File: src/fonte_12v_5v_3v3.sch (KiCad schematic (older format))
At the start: 10 parts, among them P3 12V Connector, U2 LD1117S50CTR, U3 LD1117S33CTR

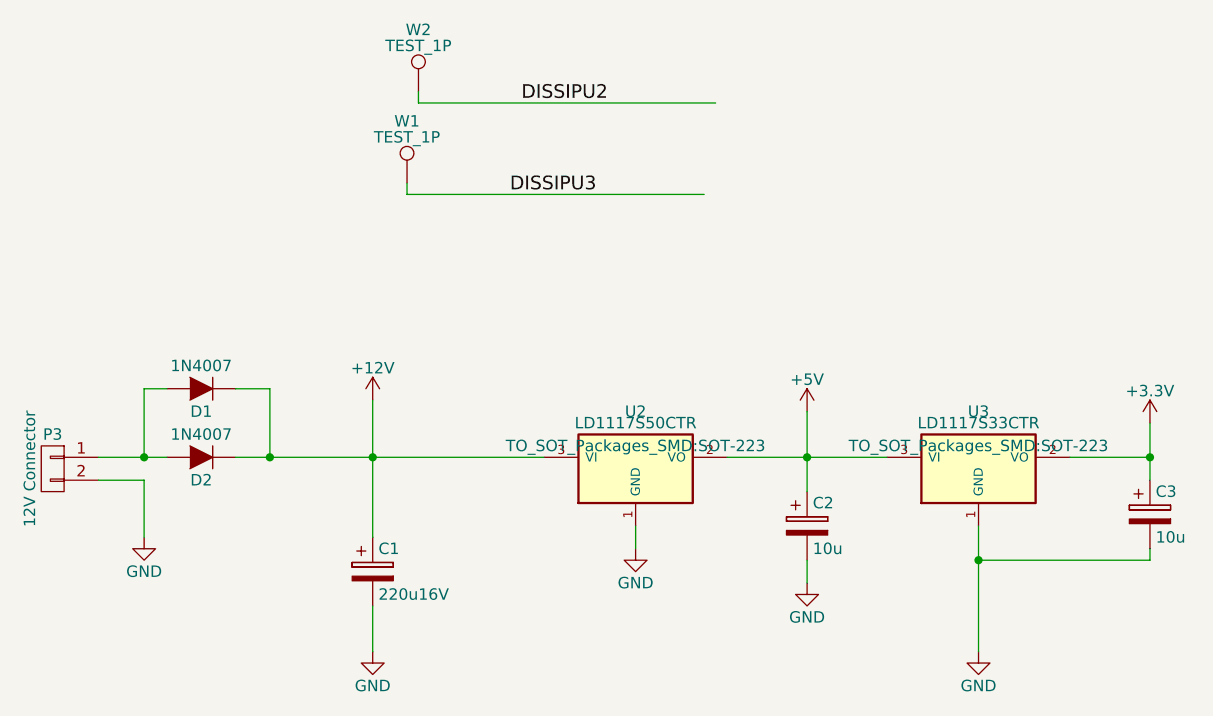
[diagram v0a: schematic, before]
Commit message: Modificacao footprint regulador 5v
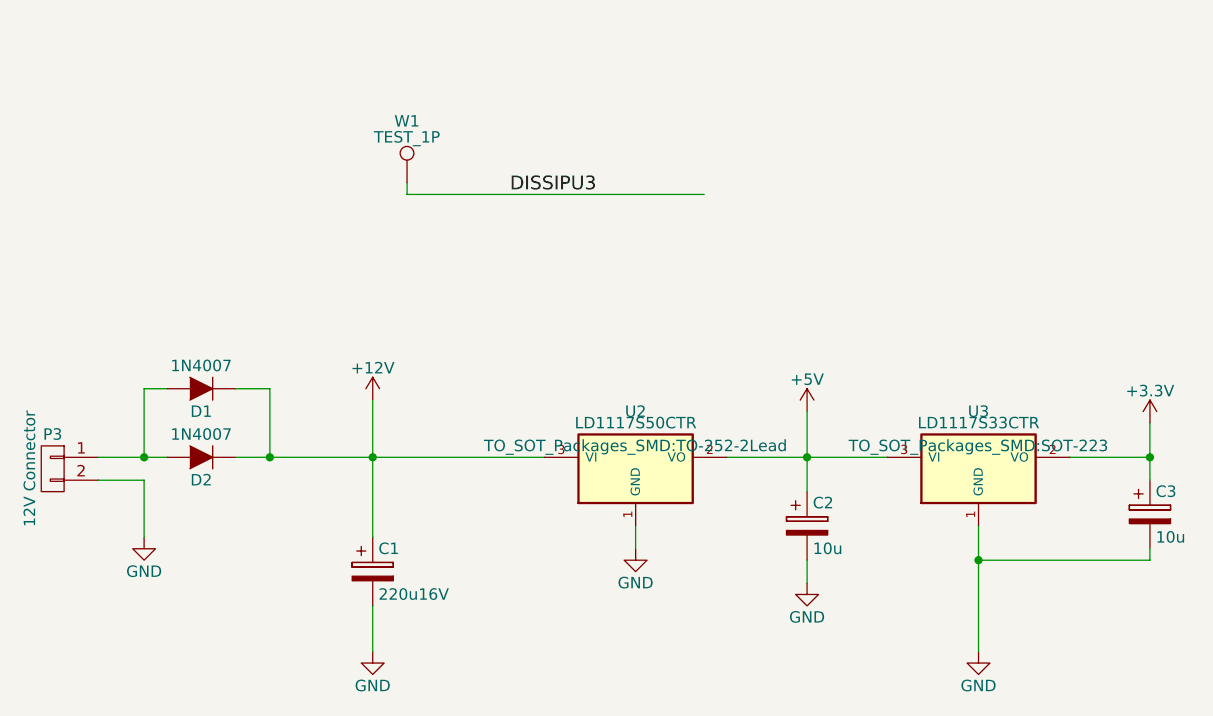
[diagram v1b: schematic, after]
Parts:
- removed W2: TEST_1P, SMD_Packages:1Pin, symbol TEST_1P
- U2: footprint TO_SOT_Packages_SMD:SOT-223 -> TO_SOT_Packages_SMD:TO-252-2Lead
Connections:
- net labels removed: DISSIPU2
- wire segments 23 -> 21
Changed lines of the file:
@@
 F 0 "U2" H 6050 3350 50  0000 C CNN
 F 1 "LD1117S50CTR" H 6050 3300 50  0000 C CNN
-F 2 "TO_SOT_Packages_SMD:SOT-223" H 6050 3200 50  0000 C CNN
+F 2 "TO_SOT_Packages_SMD:TO-252-2Lead" H 6050 3200 50  0000 C CNN
 F 3 "" H 6050 3100 50  0000 C CNN
 	1    6050 3100
@@
 Connection ~ 3900 3050
 $Comp
-L TEST_1P W2
-U 1 1 57E48B67
-P 5100 1450
-F 0 "W2" H 5100 1720 50  0000 C CNN
-F 1 "TEST_1P" H 5100 1650 50  0000 C CNN
-F 2 "SMD_Packages:1Pin" H 5300 1450 50  0001 C CNN
-F 3 "" H 5300 1450 50  0000 C CNN
-	1    5100 1450
-	1    0    0    -1
-$EndComp
-Text Label 5550 1500 0    60   ~ 0
-DISSIPU2
-Wire Wire Line
-	5100 1450 5100 1500
-Wire Wire Line
-	5100 1500 6400 1500
-$Comp
 L TEST_1P W1
